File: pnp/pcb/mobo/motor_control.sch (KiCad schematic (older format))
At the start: 48 parts, among them J1 X_MOTOR, J2 Y_MOTOR1, J3 Z_MOTOR, J37 P_MOTOR, J38 C_MOTOR, J4 R_MOTOR, J48 Y_MOTOR2

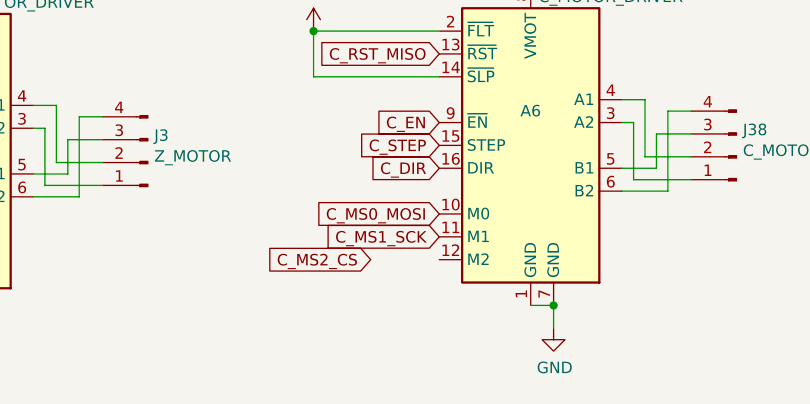
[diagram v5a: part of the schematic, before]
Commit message: a resistor was missing for one of the stepper motor drivers. added it back in, and made all resistors the same footprint.
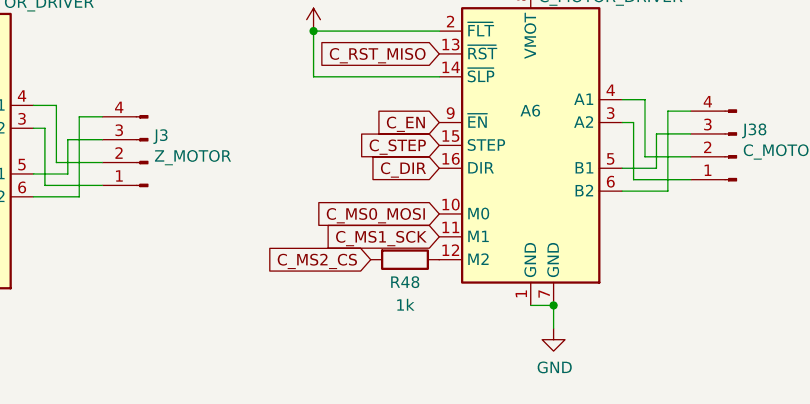
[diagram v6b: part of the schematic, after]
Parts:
- added R48: 1k, Resistor_SMD:R_0805_2012Metric_Pad1.15x1.40mm_HandSolder, symbol Device:R
- R43, R44, R45, R46, R47: footprint Resistor_SMD:R_0805_2012Metric_Pad1.20x1.40mm_HandSolder -> Resistor_SMD:R_0805_2012Metric_Pad1.15x1.40mm_HandSolder
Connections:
- net C_MS2_CS: now also R48.2
- net at A6.12 (M2): now also R48.1
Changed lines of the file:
@@
 F 0 "R47" V 4425 4875 50  0000 C CNN
 F 1 "1k" V 4525 4875 50  0000 C CNN
-F 2 "Resistor_SMD:R_0805_2012Metric_Pad1.20x1.40mm_HandSolder" V 4255 4875 50  0001 C CNN
+F 2 "Resistor_SMD:R_0805_2012Metric_Pad1.15x1.40mm_HandSolder" V 4255 4875 50  0001 C CNN
 F 3 "~" H 4325 4875 50  0001 C CNN
 	1    4325 4875
@@
 F 0 "R43" V 1500 4900 50  0000 C CNN
 F 1 "1k" V 1600 4900 50  0000 C CNN
-F 2 "Resistor_SMD:R_0805_2012Metric_Pad1.20x1.40mm_HandSolder" V 1330 4900 50  0001 C CNN
+F 2 "Resistor_SMD:R_0805_2012Metric_Pad1.15x1.40mm_HandSolder" V 1330 4900 50  0001 C CNN
 F 3 "~" H 1400 4900 50  0001 C CNN
 	1    1400 4900
@@
 F 0 "R46" V 4425 2725 50  0000 C CNN
 F 1 "1k" V 4525 2725 50  0000 C CNN
-F 2 "Resistor_SMD:R_0805_2012Metric_Pad1.20x1.40mm_HandSolder" V 4255 2725 50  0001 C CNN
+F 2 "Resistor_SMD:R_0805_2012Metric_Pad1.15x1.40mm_HandSolder" V 4255 2725 50  0001 C CNN
 F 3 "~" H 4325 2725 50  0001 C CNN
 	1    4325 2725
@@
 F 0 "R44" V 1775 2750 50  0000 C CNN
 F 1 "1k" V 1875 2750 50  0000 C CNN
-F 2 "Resistor_SMD:R_0805_2012Metric_Pad1.20x1.40mm_HandSolder" V 1605 2750 50  0001 C CNN
+F 2 "Resistor_SMD:R_0805_2012Metric_Pad1.15x1.40mm_HandSolder" V 1605 2750 50  0001 C CNN
 F 3 "~" H 1675 2750 50  0001 C CNN
 	1    1675 2750
@@
 F 0 "R45" V 1850 6950 50  0000 C CNN
 F 1 "1k" V 1950 6950 50  0000 C CNN
-F 2 "Resistor_SMD:R_0805_2012Metric_Pad1.20x1.40mm_HandSolder" V 1680 6950 50  0001 C CNN
+F 2 "Resistor_SMD:R_0805_2012Metric_Pad1.15x1.40mm_HandSolder" V 1680 6950 50  0001 C CNN
 F 3 "~" H 1750 6950 50  0001 C CNN
 	1    1750 6950
@@
 	1    0    0    -1
 $EndComp
+$Comp
+L Device:R R48
+U 1 1 5FED0D72
+P 4325 6925
+F 0 "R48" V 4425 6925 50  0000 C CNN
+F 1 "1k" V 4525 6925 50  0000 C CNN
+F 2 "Resistor_SMD:R_0805_2012Metric_Pad1.15x1.40mm_HandSolder" V 4255 6925 50  0001 C CNN
+F 3 "~" H 4325 6925 50  0001 C CNN
+	1    4325 6925
+	0    1    1    0
+$EndComp
 $EndSCHEMATC

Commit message: All fixes from #85
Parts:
- J1, J2, J3, J37, J38, J4, J48: footprint Connector_JST:JST_XH_B04B-XH-A_1x04_P2.50mm_Vertical -> Connector_JST:JST_XH_B4B-XH-A_1x04_P2.50mm_Vertical
- JP1, JP10, JP11, JP12, JP13, JP14, JP15, JP16, JP17, JP18, JP19, JP2, JP20, JP21, JP22, JP23, JP24, JP3, JP4, JP5, JP6, JP7, JP8, JP9: footprint Connector_PinSocket_2.54mm:PinSocket_1x03_P2.54mm_Vertical -> Connector_PinHeader_2.54mm:PinHeader_1x03_P2.54mm_Vertical

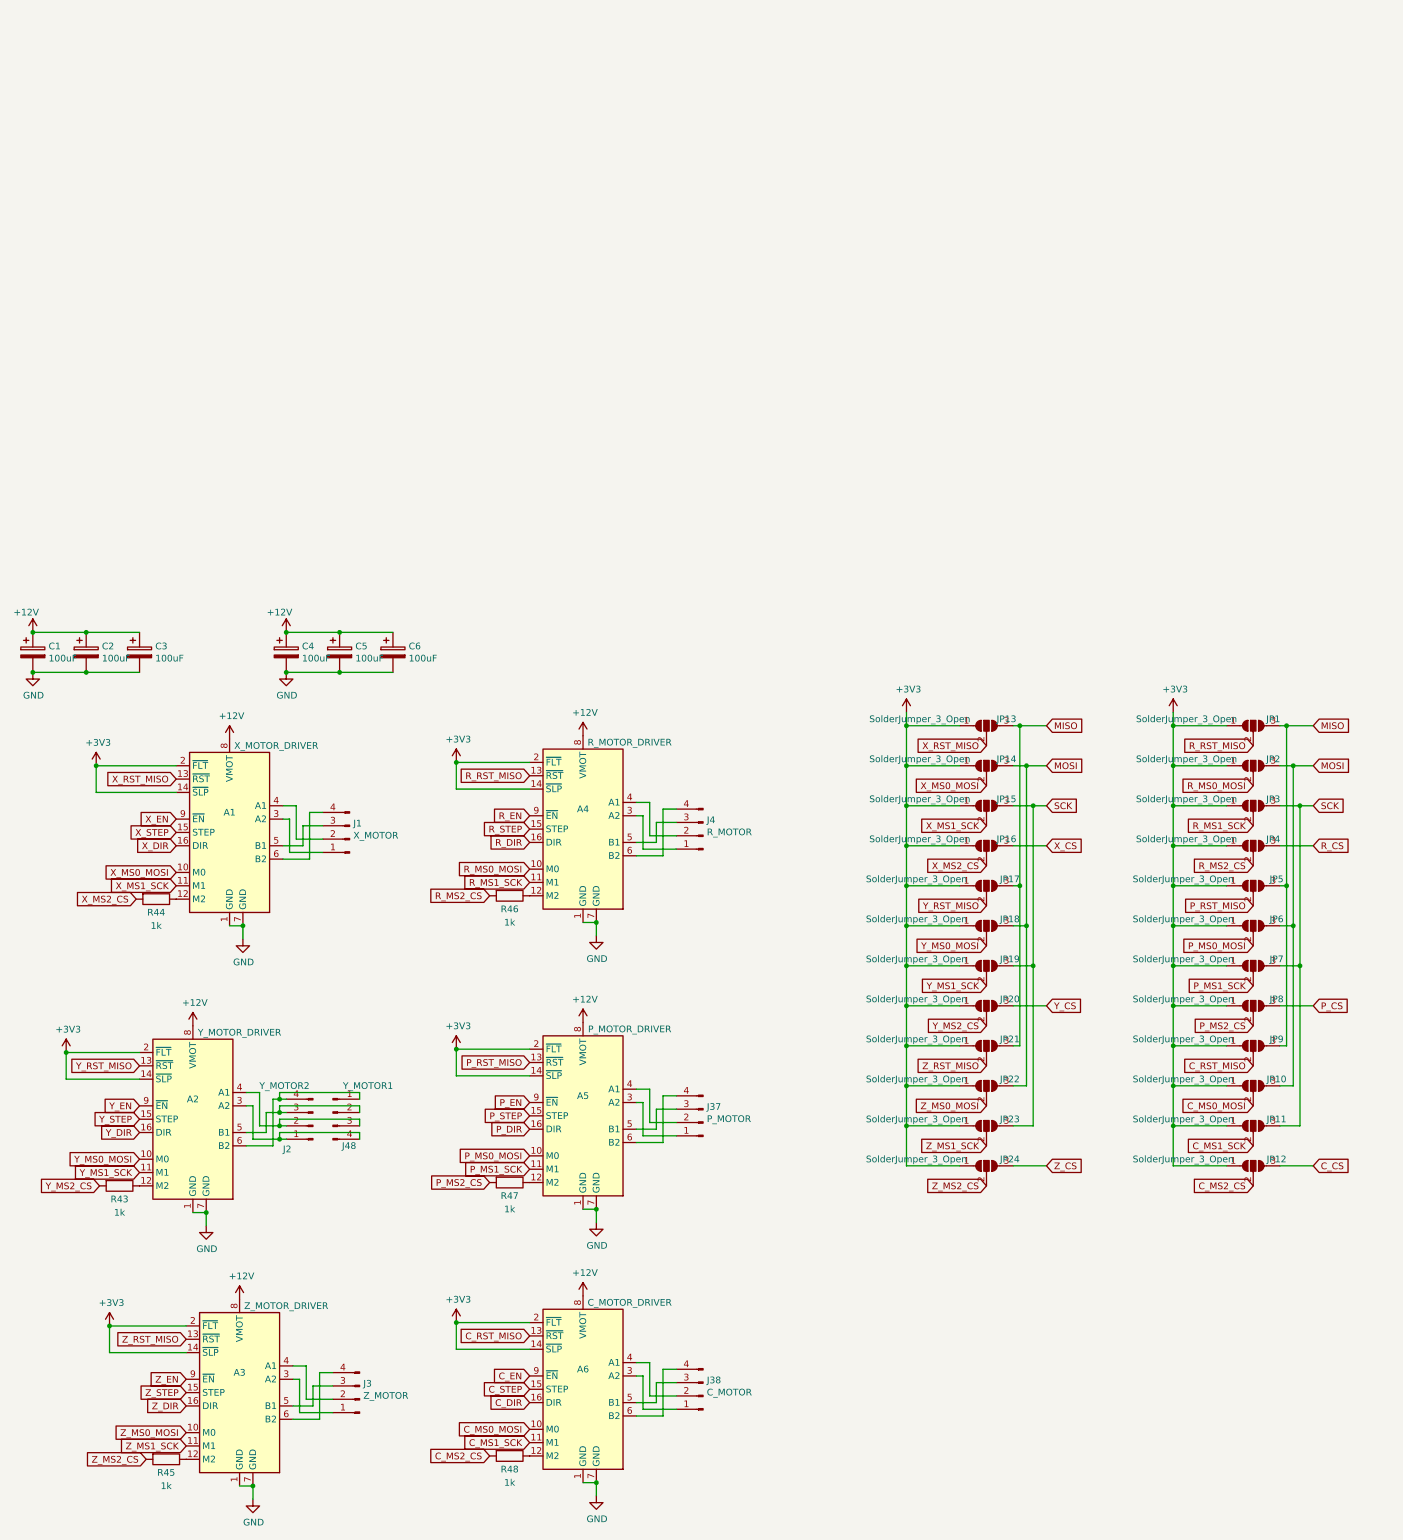
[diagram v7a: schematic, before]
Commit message: Y motores wired in parallel, change to 4 layer board and remove analog decoupling
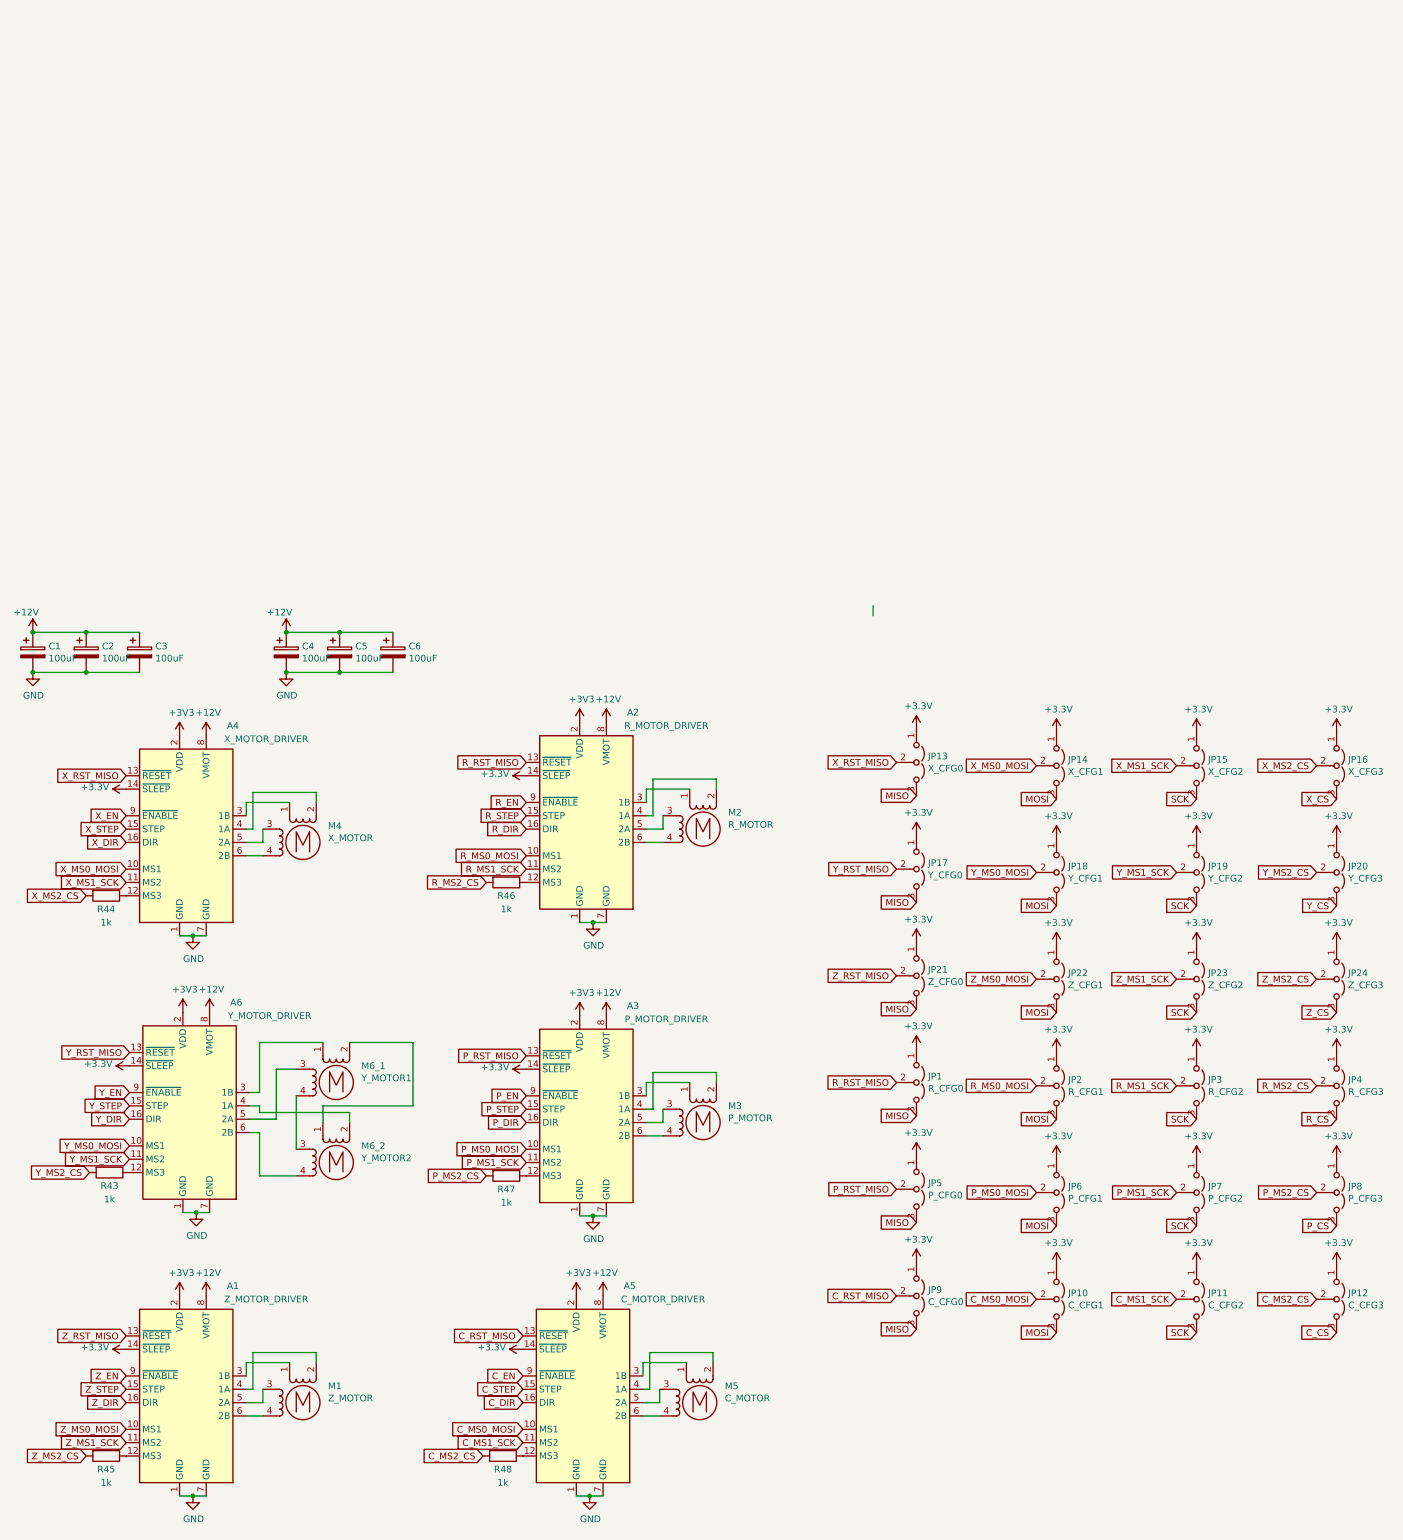
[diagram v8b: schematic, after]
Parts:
- removed A1: X_MOTOR_DRIVER, Module:Pololu_Breakout-16_15.2x20.3mm, symbol Driver_Motor:Pololu_Breakout_DRV8825
- removed A2: Y_MOTOR_DRIVER, Module:Pololu_Breakout-16_15.2x20.3mm, symbol Driver_Motor:Pololu_Breakout_DRV8825
- removed A3: Z_MOTOR_DRIVER, Module:Pololu_Breakout-16_15.2x20.3mm, symbol Driver_Motor:Pololu_Breakout_DRV8825
- removed A4: R_MOTOR_DRIVER, Module:Pololu_Breakout-16_15.2x20.3mm, symbol Driver_Motor:Pololu_Breakout_DRV8825
- removed A5: P_MOTOR_DRIVER, Module:Pololu_Breakout-16_15.2x20.3mm, symbol Driver_Motor:Pololu_Breakout_DRV8825
- removed A6: C_MOTOR_DRIVER, Module:Pololu_Breakout-16_15.2x20.3mm, symbol Driver_Motor:Pololu_Breakout_DRV8825
- removed J1: X_MOTOR, Connector_JST:JST_XH_B4B-XH-A_1x04_P2.50mm_Vertical, symbol Connector:Conn_01x04_Male
- removed J2: Y_MOTOR1, Connector_JST:JST_XH_B4B-XH-A_1x04_P2.50mm_Vertical, symbol Connector:Conn_01x04_Male
- removed J3: Z_MOTOR, Connector_JST:JST_XH_B4B-XH-A_1x04_P2.50mm_Vertical, symbol Connector:Conn_01x04_Male
- removed J37: P_MOTOR, Connector_JST:JST_XH_B4B-XH-A_1x04_P2.50mm_Vertical, symbol Connector:Conn_01x04_Male
- removed J38: C_MOTOR, Connector_JST:JST_XH_B4B-XH-A_1x04_P2.50mm_Vertical, symbol Connector:Conn_01x04_Male
- removed J4: R_MOTOR, Connector_JST:JST_XH_B4B-XH-A_1x04_P2.50mm_Vertical, symbol Connector:Conn_01x04_Male
- removed J48: Y_MOTOR2, Connector_JST:JST_XH_B4B-XH-A_1x04_P2.50mm_Vertical, symbol Connector:Conn_01x04_Male
- removed JP1, JP10, JP11, JP12, JP13, JP14, JP15, JP16, JP17, JP18, JP19, JP2, JP20, JP21, JP22, JP23, JP24, JP3, JP4, JP5, JP6, JP7, JP8, JP9: SolderJumper_3_Open, Connector_PinHeader_2.54mm:PinHeader_1x03_P2.54mm_Vertical, symbol Jumper:SolderJumper_3_Open
- added A1: Z_MOTOR_DRIVER, Module:Pololu_Breakout-16_15.2x20.3mm, symbol Driver_Motor:Pololu_Breakout_A4988
- added A2: R_MOTOR_DRIVER, Module:Pololu_Breakout-16_15.2x20.3mm, symbol Driver_Motor:Pololu_Breakout_A4988
- added A3: P_MOTOR_DRIVER, Module:Pololu_Breakout-16_15.2x20.3mm, symbol Driver_Motor:Pololu_Breakout_A4988
- added A4: X_MOTOR_DRIVER, Module:Pololu_Breakout-16_15.2x20.3mm, symbol Driver_Motor:Pololu_Breakout_A4988
- added A5: C_MOTOR_DRIVER, Module:Pololu_Breakout-16_15.2x20.3mm, symbol Driver_Motor:Pololu_Breakout_A4988
- added A6: Y_MOTOR_DRIVER, Module:Pololu_Breakout-16_15.2x20.3mm, symbol Driver_Motor:Pololu_Breakout_A4988
- added JP1: R_CFG0, Connector_PinHeader_2.54mm:PinHeader_1x03_P2.54mm_Vertical, symbol Jumper:Jumper_3_Open
- added JP10: C_CFG1, Connector_PinHeader_2.54mm:PinHeader_1x03_P2.54mm_Vertical, symbol Jumper:Jumper_3_Open
- added JP11: C_CFG2, Connector_PinHeader_2.54mm:PinHeader_1x03_P2.54mm_Vertical, symbol Jumper:Jumper_3_Open
- added JP12: C_CFG3, Connector_PinHeader_2.54mm:PinHeader_1x03_P2.54mm_Vertical, symbol Jumper:Jumper_3_Open
- added JP13: X_CFG0, Connector_PinHeader_2.54mm:PinHeader_1x03_P2.54mm_Vertical, symbol Jumper:Jumper_3_Open
- added JP14: X_CFG1, Connector_PinHeader_2.54mm:PinHeader_1x03_P2.54mm_Vertical, symbol Jumper:Jumper_3_Open
- added JP15: X_CFG2, Connector_PinHeader_2.54mm:PinHeader_1x03_P2.54mm_Vertical, symbol Jumper:Jumper_3_Open
- added JP16: X_CFG3, Connector_PinHeader_2.54mm:PinHeader_1x03_P2.54mm_Vertical, symbol Jumper:Jumper_3_Open
- added JP17: Y_CFG0, Connector_PinHeader_2.54mm:PinHeader_1x03_P2.54mm_Vertical, symbol Jumper:Jumper_3_Open
- added JP18: Y_CFG1, Connector_PinHeader_2.54mm:PinHeader_1x03_P2.54mm_Vertical, symbol Jumper:Jumper_3_Open
- added JP19: Y_CFG2, Connector_PinHeader_2.54mm:PinHeader_1x03_P2.54mm_Vertical, symbol Jumper:Jumper_3_Open
- added JP2: R_CFG1, Connector_PinHeader_2.54mm:PinHeader_1x03_P2.54mm_Vertical, symbol Jumper:Jumper_3_Open
- added JP20: Y_CFG3, Connector_PinHeader_2.54mm:PinHeader_1x03_P2.54mm_Vertical, symbol Jumper:Jumper_3_Open
- added JP21: Z_CFG0, Connector_PinHeader_2.54mm:PinHeader_1x03_P2.54mm_Vertical, symbol Jumper:Jumper_3_Open
- added JP22: Z_CFG1, Connector_PinHeader_2.54mm:PinHeader_1x03_P2.54mm_Vertical, symbol Jumper:Jumper_3_Open
- added JP23: Z_CFG2, Connector_PinHeader_2.54mm:PinHeader_1x03_P2.54mm_Vertical, symbol Jumper:Jumper_3_Open
- added JP24: Z_CFG3, Connector_PinHeader_2.54mm:PinHeader_1x03_P2.54mm_Vertical, symbol Jumper:Jumper_3_Open
- added JP3: R_CFG2, Connector_PinHeader_2.54mm:PinHeader_1x03_P2.54mm_Vertical, symbol Jumper:Jumper_3_Open
- added JP4: R_CFG3, Connector_PinHeader_2.54mm:PinHeader_1x03_P2.54mm_Vertical, symbol Jumper:Jumper_3_Open
- added JP5: P_CFG0, Connector_PinHeader_2.54mm:PinHeader_1x03_P2.54mm_Vertical, symbol Jumper:Jumper_3_Open
- added JP6: P_CFG1, Connector_PinHeader_2.54mm:PinHeader_1x03_P2.54mm_Vertical, symbol Jumper:Jumper_3_Open
- added JP7: P_CFG2, Connector_PinHeader_2.54mm:PinHeader_1x03_P2.54mm_Vertical, symbol Jumper:Jumper_3_Open
- added JP8: P_CFG3, Connector_PinHeader_2.54mm:PinHeader_1x03_P2.54mm_Vertical, symbol Jumper:Jumper_3_Open
- added JP9: C_CFG0, Connector_PinHeader_2.54mm:PinHeader_1x03_P2.54mm_Vertical, symbol Jumper:Jumper_3_Open
- added M1: Z_MOTOR, Connector_JST:JST_XH_B4B-XH-A_1x04_P2.50mm_Vertical, symbol Motor:Stepper_Motor_bipolar
- added M2: R_MOTOR, Connector_JST:JST_XH_B4B-XH-A_1x04_P2.50mm_Vertical, symbol Motor:Stepper_Motor_bipolar
- added M3: P_MOTOR, Connector_JST:JST_XH_B4B-XH-A_1x04_P2.50mm_Vertical, symbol Motor:Stepper_Motor_bipolar
- added M4: X_MOTOR, Connector_JST:JST_XH_B4B-XH-A_1x04_P2.50mm_Vertical, symbol Motor:Stepper_Motor_bipolar
- added M5: C_MOTOR, Connector_JST:JST_XH_B4B-XH-A_1x04_P2.50mm_Vertical, symbol Motor:Stepper_Motor_bipolar
- added M6_1: Y_MOTOR1, Connector_JST:JST_XH_B4B-XH-A_1x04_P2.50mm_Vertical, symbol Motor:Stepper_Motor_bipolar
- added M6_2: Y_MOTOR2, Connector_JST:JST_XH_B4B-XH-A_1x04_P2.50mm_Vertical, symbol Motor:Stepper_Motor_bipolar
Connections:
- net +12V: now also A1.8 (VMOT), A2.8 (VMOT), A3.8 (VMOT), A4.8 (VMOT), A5.8 (VMOT), A6.8 (VMOT)
- net +3V3: now also A1.14 (~SLEEP), A1.2 (VDD), A2.14 (~SLEEP), A2.2 (VDD), A3.14 (~SLEEP), A3.2 (VDD), A4.14 (~SLEEP), A4.2 (VDD), A5.14 (~SLEEP), A5.2 (VDD), A6.14 (~SLEEP), A6.2 (VDD), JP1.1 (A), JP10.1 (A), JP11.1 (A), JP12.1 (A), JP13.1 (A), JP14.1 (A), JP15.1 (A), JP16.1 (A), JP17.1 (A), JP18.1 (A), JP19.1 (A), JP2.1 (A), JP20.1 (A), JP21.1 (A), JP22.1 (A), JP23.1 (A), JP24.1 (A), JP3.1 (A), JP4.1 (A), JP5.1 (A), JP6.1 (A), JP7.1 (A), JP8.1 (A), JP9.1 (A)
- net C_CS: now also JP12.3 (B)
- net C_DIR: now also A5.16 (DIR)
- net C_EN: now also A5.9 (~ENABLE)
- net C_MS0_MOSI: now also A5.10 (MS1), JP10.2 (C)
- net C_MS1_SCK: now also A5.11 (MS2), JP11.2 (C)
- net C_MS2_CS: now also JP12.2 (C)
- net C_RST_MISO: now also A5.13 (~RESET), JP9.2 (C)
- net C_STEP: now also A5.15 (STEP)
- net GND: now also A1.1 (GND), A1.7 (GND), A2.1 (GND), A2.7 (GND), A3.1 (GND), A3.7 (GND), A4.1 (GND), A4.7 (GND), A5.1 (GND), A5.7 (GND), A6.1 (GND), A6.7 (GND)
- net MISO: now also JP1.3 (B), JP13.3 (B), JP17.3 (B), JP21.3 (B), JP5.3 (B), JP9.3 (B)
- net MOSI: now also JP10.3 (B), JP14.3 (B), JP18.3 (B), JP2.3 (B), JP22.3 (B), JP6.3 (B)
- net P_CS: now also JP8.3 (B)
- net P_DIR: now also A3.16 (DIR)
- net P_EN: now also A3.9 (~ENABLE)
- net P_MS0_MOSI: now also A3.10 (MS1), JP6.2 (C)
- net P_MS1_SCK: now also A3.11 (MS2), JP7.2 (C)
- net P_MS2_CS: now also JP8.2 (C)
- net P_RST_MISO: now also A3.13 (~RESET), JP5.2 (C)
- net P_STEP: now also A3.15 (STEP)
- net R_CS: now also JP4.3 (B)
- net R_DIR: now also A2.16 (DIR)
- net R_EN: now also A2.9 (~ENABLE)
- net R_MS0_MOSI: now also A2.10 (MS1), JP2.2 (C)
- net R_MS1_SCK: now also A2.11 (MS2), JP3.2 (C)
- net R_MS2_CS: now also JP4.2 (C)
- net R_RST_MISO: now also A2.13 (~RESET), JP1.2 (C)
- net R_STEP: now also A2.15 (STEP)
- net SCK: now also JP11.3 (B), JP15.3 (B), JP19.3 (B), JP23.3 (B), JP3.3 (B), JP7.3 (B)
- net X_CS: now also JP16.3 (B)
- net X_DIR: now also A4.16 (DIR)
- net X_EN: now also A4.9 (~ENABLE)
- net X_MS0_MOSI: now also A4.10 (MS1), JP14.2 (C)
- net X_MS1_SCK: now also A4.11 (MS2), JP15.2 (C)
- net X_MS2_CS: now also JP16.2 (C)
- net X_RST_MISO: now also A4.13 (~RESET), JP13.2 (C)
- net X_STEP: now also A4.15 (STEP)
- net Y_CS: now also JP20.3 (B)
- net Y_DIR: now also A6.16 (DIR)
- net Y_EN: now also A6.9 (~ENABLE)
- net Y_MS0_MOSI: now also A6.10 (MS1), JP18.2 (C)
- net Y_MS1_SCK: now also A6.11 (MS2), JP19.2 (C)
- net Y_MS2_CS: now also JP20.2 (C)
- net Y_RST_MISO: now also A6.13 (~RESET), JP17.2 (C)
- net Y_STEP: now also A6.15 (STEP)
- net Z_CS: now also JP24.3 (B)
- net Z_DIR: now also A1.16 (DIR)
- net Z_EN: now also A1.9 (~ENABLE)
- net Z_MS0_MOSI: now also A1.10 (MS1), JP22.2 (C)
- net Z_MS1_SCK: now also A1.11 (MS2), JP23.2 (C)
- net Z_MS2_CS: now also JP24.2 (C)
- net Z_RST_MISO: now also A1.13 (~RESET), JP21.2 (C)
- net Z_STEP: now also A1.15 (STEP)
- net at R45.1: now also A1.12 (MS3)
- net at R44.1: now also A4.12 (MS3)
- net at R43.1: now also A6.12 (MS3)
- net at R48.1: now also A5.12 (MS3)
- net at R46.1: now also A2.12 (MS3)
- net at R47.1: now also A3.12 (MS3)
- new net: A2.3 (1B), M2.1
- new net: A2.4 (1A), M2.2 (-)
- new net: A2.5 (2A), M2.3
- new net: A2.6 (2B), M2.4
- new net: A4.3 (1B), M4.1
- new net: A4.4 (1A), M4.2 (-)
- new net: A4.5 (2A), M4.3
- new net: A4.6 (2B), M4.4
- new net: A6.3 (1B), M6_1.1
- new net: A6.4 (1A), M6_2.2 (-)
- new net: A6.5 (2A), M6_1.3
- new net: A6.6 (2B), M6_2.4
- new net: M6_1.2 (-), M6_2.1
- new net: M6_1.4, M6_2.3
- new net: A3.3 (1B), M3.1
- new net: A3.4 (1A), M3.2 (-)
- new net: A3.5 (2A), M3.3
- new net: A3.6 (2B), M3.4
- new net: A5.3 (1B), M5.1
- new net: A5.4 (1A), M5.2 (-)
- new net: A5.5 (2A), M5.3
- new net: A5.6 (2B), M5.4
- new net: A1.3 (1B), M1.1
- new net: A1.4 (1A), M1.2 (-)
- new net: A1.5 (2A), M1.3
- new net: A1.6 (2B), M1.4
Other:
- moved on the sheet: R43, R44, R45, R46, R47, R48
